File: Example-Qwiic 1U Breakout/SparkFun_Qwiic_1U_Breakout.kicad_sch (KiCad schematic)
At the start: 37 parts, among them J1 Qwiic_RA, J2 Qwiic_RA, J3 Conn_01x06, Q1 BSS138, Q2 BSS138, U1 AP3012

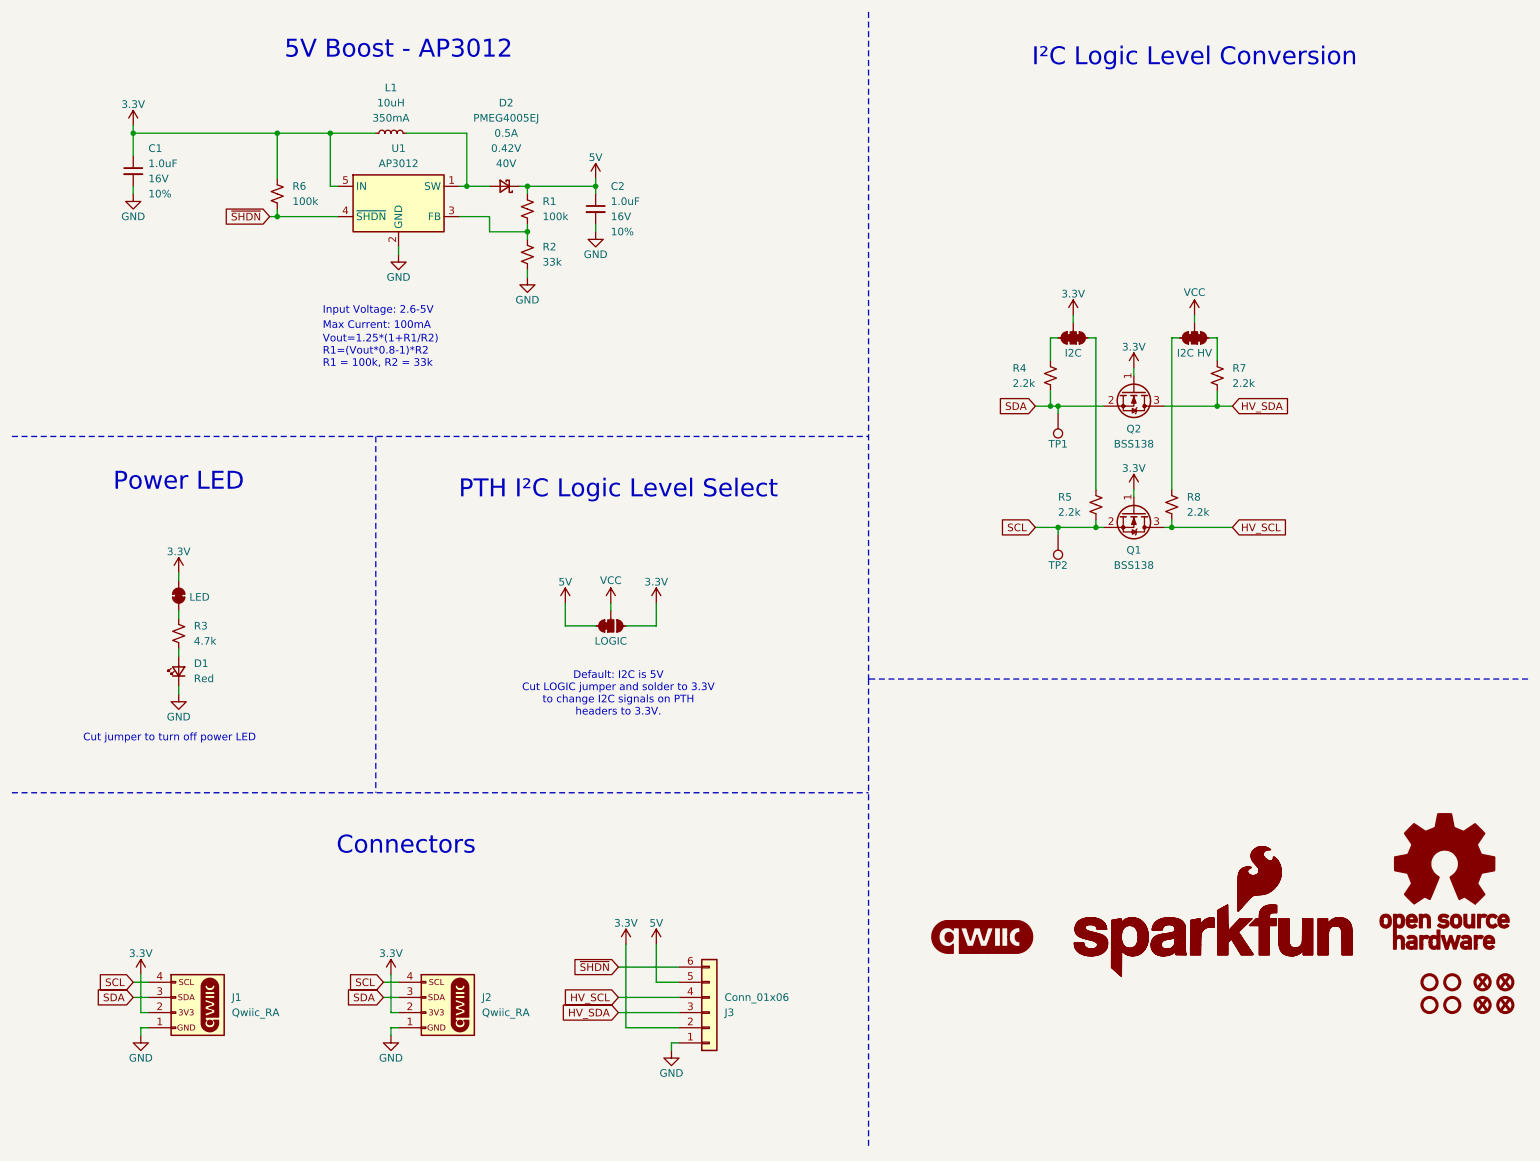
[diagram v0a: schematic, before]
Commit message: Update examples to KiCad v9
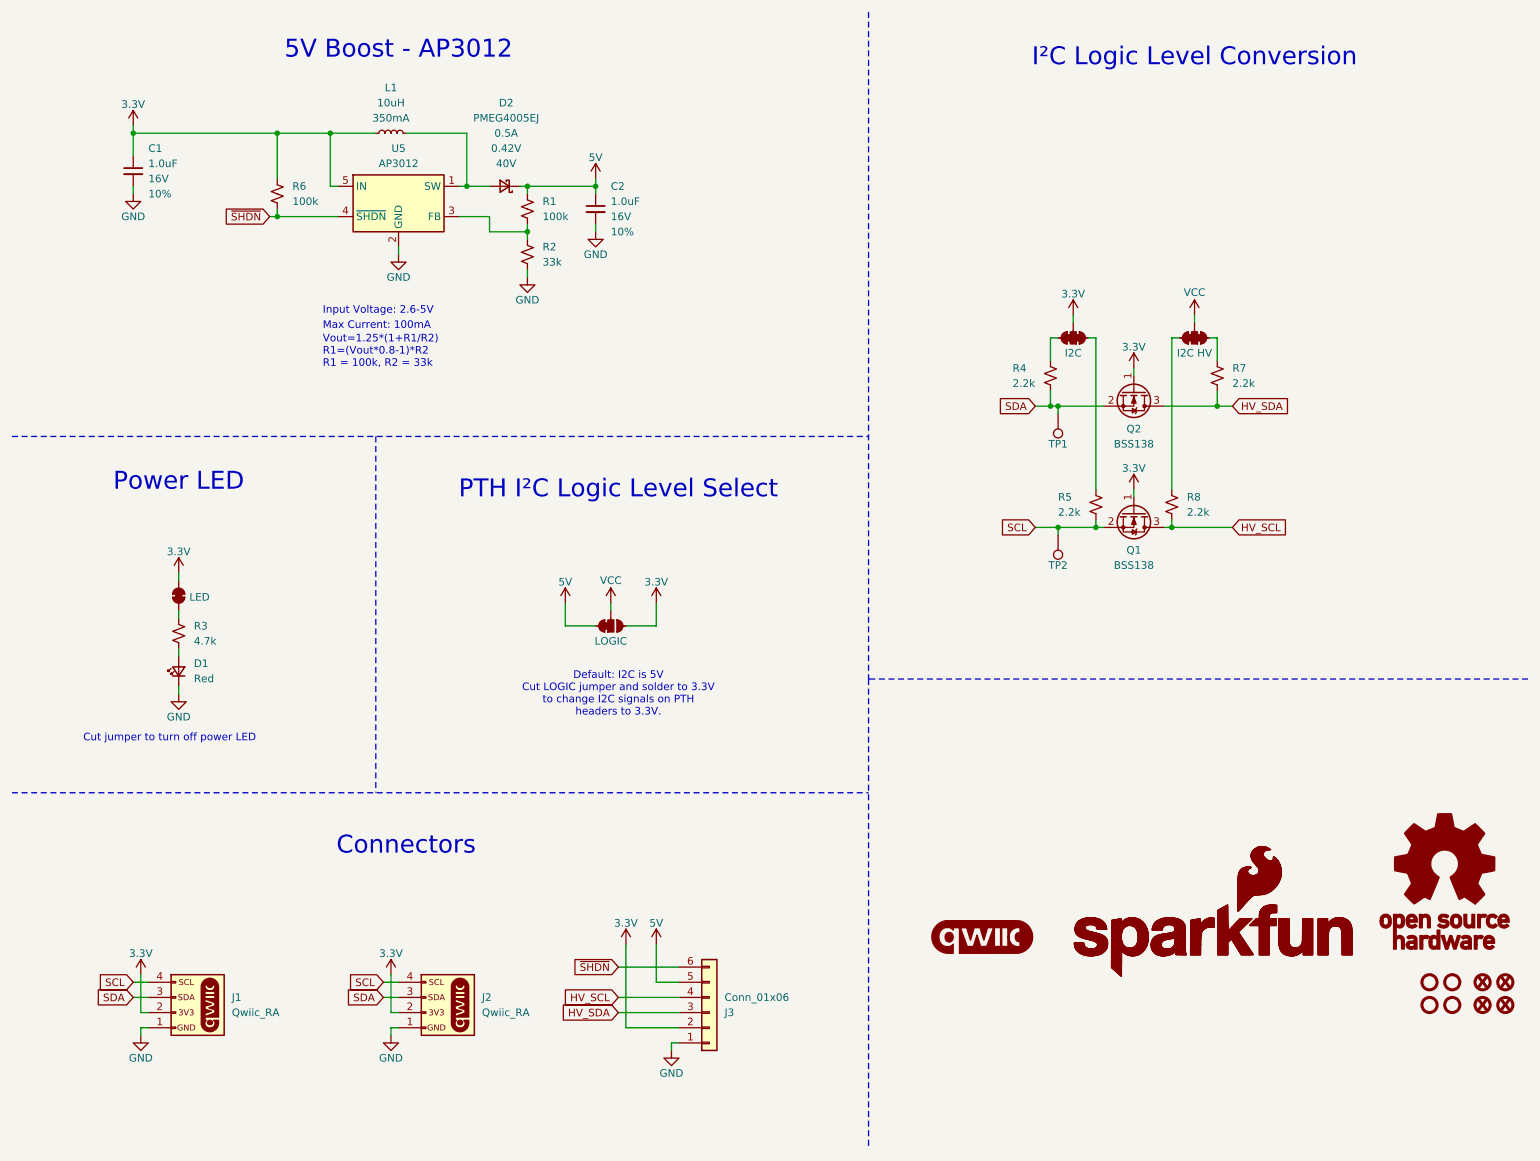
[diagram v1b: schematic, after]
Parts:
- renumbered U1 to U5
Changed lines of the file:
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@@
 (kicad_sch
-	(version 20231120)
+	(version 20250114)
 	(generator "eeschema")
-	(generator_version "8.0")
+	(generator_version "9.0")
 	(paper "USLetter")
 	(title_block
@@
 		(comment 3 "Designed by: P. Lewis")
 	)
+	(text "Input Voltage: 2.6-5V"
+		(exclude_from_sim no)
+		(at 64.77 63.5 0)
+		(effects
+			(font
+				(size 1.27 1.27)
+				(color 132 132 132 1)
+			)
+			(justify left bottom)
+		)
+	)
+	(text "Vout=1.25*(1+R1/R2)\nR1=(Vout*0.8-1)*R2\nR1 = 100k, R2 = 33k"
+		(exclude_from_sim no)
+		(at 64.77 72.39 0)
+		(effects
+			(font
+				(size 1.27 1.27)
+				(color 132 132 132 1)
+			)
+			(justify left bottom)
+		)
+	)
+	(text "Default: I2C is 5V\nCut LOGIC jumper and solder to 3.3V\nto change I2C signals on PTH \nheaders to 3.3V."
+		(exclude_from_sim no)
+		(at 114.3 127 0)
+		(effects
+			(font
+				(size 1.27 1.27)
+				(color 132 132 132 1)
+			)
+		)
+	)
+	(text "I²C Logic Level Conversion"
+		(exclude_from_sim no)
+		(at 210.82 20.32 0)
+		(effects
+			(font
+				(size 3 3)
+			)
+		)
+	)
+	(text "Max Current: 100mA"
+		(exclude_from_sim no)
+		(at 64.77 66.04 0)
+		(effects
+			(font
+				(size 1.27 1.27)
+				(color 132 132 132 1)
+			)
+			(justify left bottom)
+		)
+	)
+	(text "Cut jumper to turn off power LED"
+		(exclude_from_sim no)
+		(at 24.638 135.128 0)
+		(effects
+			(font
+				(size 1.27 1.27)
+				(color 132 132 132 1)
+			)
+			(justify left bottom)
+		)
+	)
+	(text "Power LED"
+		(exclude_from_sim no)
+		(at 40.64 91.44 0)
+		(effects
+			(font
+				(size 3 3)
+			)
+		)
+	)
+	(text "Connectors"
+		(exclude_from_sim no)
+		(at 78.74 152.4 0)
+		(effects
+			(font
+				(size 3 3)
+			)
+		)
+	)
+	(text "PTH I²C Logic Level Select"
+		(exclude_from_sim no)
+		(at 114.3 92.71 0)
+		(effects
+			(font
+				(size 3 3)
+			)
+		)
+	)
+	(text "5V Boost - AP3012"
+		(exclude_from_sim no)
+		(at 77.47 19.05 0)
+		(effects
+			(font
+				(size 3 3)
+			)
+		)
+	)
 	(junction
 		(at 99.06 49.53)
@@
 		)
 	)
-	(text "Input Voltage: 2.6-5V"
-		(exclude_from_sim no)
-		(at 64.77 63.5 0)
-		(effects
-			(font
-				(size 1.27 1.27)
-				(color 132 132 132 1)
-			)
-			(justify left bottom)
-		)
-	)
-	(text "Vout=1.25*(1+R1/R2)\nR1=(Vout*0.8-1)*R2\nR1 = 100k, R2 = 33k"
-		(exclude_from_sim no)
-		(at 64.77 72.39 0)
-		(effects
-			(font
-				(size 1.27 1.27)
-				(color 132 132 132 1)
-			)
-			(justify left bottom)
-		)
-	)
-	(text "Default: I2C is 5V\nCut LOGIC jumper and solder to 3.3V\nto change I2C signals on PTH \nheaders to 3.3V."
-		(exclude_from_sim no)
-		(at 114.3 127 0)
-		(effects
-			(font
-				(size 1.27 1.27)
-				(color 132 132 132 1)
-			)
-		)
-	)
-	(text "I²C Logic Level Conversion"
-		(exclude_from_sim no)
-		(at 210.82 20.32 0)
-		(effects
-			(font
-				(size 3 3)
-			)
-		)
-	)
-	(text "Max Current: 100mA"
-		(exclude_from_sim no)
-		(at 64.77 66.04 0)
-		(effects
-			(font
-				(size 1.27 1.27)
-				(color 132 132 132 1)
-			)
-			(justify left bottom)
-		)
-	)
-	(text "Cut jumper to turn off power LED"
-		(exclude_from_sim no)
-		(at 24.638 135.128 0)
-		(effects
-			(font
-				(size 1.27 1.27)
-				(color 132 132 132 1)
-			)
-			(justify left bottom)
-		)
-	)
-	(text "Power LED"
-		(exclude_from_sim no)
-		(at 40.64 91.44 0)
-		(effects
-			(font
-				(size 3 3)
-			)
-		)
-	)
-	(text "Connectors"
-		(exclude_from_sim no)
-		(at 78.74 152.4 0)
-		(effects
-			(font
-				(size 3 3)
-			)
-		)
-	)
-	(text "PTH I²C Logic Level Select"
-		(exclude_from_sim no)
-		(at 114.3 92.71 0)
-		(effects
-			(font
-				(size 3 3)
-			)
-		)
-	)
-	(text "5V Boost - AP3012"
-		(exclude_from_sim no)
-		(at 77.47 19.05 0)
-		(effects
-			(font
-				(size 3 3)
-			)
-		)
-	)
 	(global_label "HV_SDA"
 		(shape input)
@@
 		(on_board yes)
 		(dnp no)
-		(property "Reference" "#PWR03"
+		(property "Reference" "#PWR0109"
 			(at 77.47 59.69 0)
 			(effects
@@
 		(on_board yes)
 		(dnp no)
-		(property "Reference" "#PWR04"
+		(property "Reference" "#PWR0101"
 			(at 99.06 63.5 0)
 			(effects
@@
 		(on_board yes)
 		(dnp no)
-		(property "Reference" "#PWR0124"
+		(property "Reference" "#PWR0107"
 			(at 123.19 193.04 0)
 			(effects
@@
 		(dnp no)
 		(fields_autoplaced yes)
-		(property "Reference" "U1"
+		(property "Reference" "U5"
 			(at 77.47 35.56 0)
 			(effects
@@
 		(on_board yes)
 		(dnp no)
-		(property "Reference" "#PWR0124"
+		(property "Reference" "#PWR0123"
 			(at 34.29 190.5 0)
 			(effects
@@
 		(on_board yes)
 		(dnp no)
-		(property "Reference" "#PWR0124"
+		(property "Reference" "#PWR0105"
 			(at 76.2 190.5 0)
 			(effects
@@
 		(on_board yes)
 		(dnp no)
-		(property "Reference" "#PWR05"
+		(property "Reference" "#PWR0102"
 			(at 110.49 55.88 0)
 			(effects
@@
 		(on_board yes)
 		(dnp no)
-		(property "Reference" "#PWR02"
+		(property "Reference" "#PWR0110"
 			(at 33.02 49.53 0)
 			(effects
@@
 		)
 	)
+	(embedded_fonts no)
 )

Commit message: Make text gray. Superscript 2s. Add company name.
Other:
- note added: "5V Boost"
- note added: "Default: I²C is 5V Cut LOGIC jumper and solder to 3.3V to change I²C signals on PTH headers to 3.3V."
- note removed: "5V Boost - AP3012"
- note removed: "Default: I2C is 5V Cut LOGIC jumper and solder to 3.3V to change I2C signals on PTH headers to 3.3V."
- note removed: "PTH I²C Logic Level Select"
- company: (none) -> SparkFun Electronics
- moved on the sheet: C1, C2, D1, D2, J1, J2, J3, Q1, Q2, R1, R2, R3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

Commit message: Update examples with latest parts
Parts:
- J1, J2: footprint SparkFun-Connector:JST_SMD_1.0mm-4_Black -> SparkFun-Connector:JST_1x04_P1.0mm_Horizontal_SMD; symbol SparkFun-Connector:Qwiic_Right_Angle -> SparkFun-Connector:Qwiic_Horizontal
- J3: footprint SparkFun-Connector:1x06 -> SparkFun-Connector:1x06_P2.54mm; symbol SparkFun-Connector:Conn_01x06 -> SparkFun-Connector:Conn_01x06_P2.54mm
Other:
- note added: "Voltage Selection"
- moved on the sheet: J1
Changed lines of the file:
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@@
 		(effects
 			(font
-				(size 2.54 2.54)
+				(size 3 3)
 			)
 		)
@@
 		(effects
 			(font
-				(size 2.54 2.54)
+				(size 3 3)
 			)
 		)
@@
 		(effects
 			(font
-				(size 2.54 2.54)
+				(size 3 3)
 			)
 		)
@@
 		(effects
 			(font
-				(size 2.54 2.54)
+				(size 3 3)
+			)
+		)
+	)
+	(text "Voltage Selection"
+		(exclude_from_sim no)
+		(at 113.03 92.71 0)
+		(effects
+			(font
+				(size 3 3)
 			)
 		)
@@
 	(wire
 		(pts
-			(xy 43.18 179.07) (xy 41.91 179.07)
+			(xy 36.83 179.07) (xy 35.56 179.07)
 		)
 		(stroke
@@
 	(wire
 		(pts
-			(xy 40.64 173.99) (xy 43.18 173.99)
+			(xy 34.29 173.99) (xy 36.83 173.99)
 		)
 		(stroke
@@
 	(wire
 		(pts
-			(xy 43.18 176.53) (xy 41.91 176.53)
+			(xy 36.83 176.53) (xy 35.56 176.53)
 		)
 		(stroke
@@
 	(wire
 		(pts
-			(xy 40.64 171.45) (xy 43.18 171.45)
+			(xy 34.29 171.45) (xy 36.83 171.45)
 		)
 		(stroke
@@
 	(wire
 		(pts
-			(xy 41.91 170.18) (xy 41.91 176.53)
+			(xy 35.56 170.18) (xy 35.56 176.53)
 		)
 		(stroke
@@
 	(wire
 		(pts
-			(xy 41.91 179.07) (xy 41.91 180.34)
+			(xy 35.56 179.07) (xy 35.56 180.34)
 		)
 		(stroke
@@
 	(global_label "SCL"
 		(shape input)
-		(at 40.64 171.45 180)
+		(at 34.29 171.45 180)
 		(fields_autoplaced yes)
 		(effects
@@
 		)
 		(property "Intersheetrefs" "${INTERSHEET_REFS}"
-			(at 34.1472 171.45 0)
+			(at 27.7972 171.45 0)
 			(effects
 				(font
@@
 	(global_label "SDA"
 		(shape input)
-		(at 40.64 173.99 180)
+		(at 34.29 173.99 180)
 		(fields_autoplaced yes)
 		(effects
@@
 		)
 		(property "Intersheetrefs" "${INTERSHEET_REFS}"
-			(at 34.0867 173.99 0)
+			(at 27.7367 173.99 0)
 			(effects
 				(font
@@
 	)
 	(symbol
-		(lib_id "SparkFun-Connector:Conn_01x06")
+		(lib_id "SparkFun-Connector:Conn_01x06_P2.54mm")
 		(at 113.03 173.99 0)
 		(mirror x)
@@
 			)
 		)
-		(property "Footprint" "SparkFun-Connector:1x06"
+		(property "Footprint" "SparkFun-Connector:1x06_P2.54mm"
 			(at 113.03 161.29 0)
 			(effects
@@
 			)
 		)
-		(property "Datasheet" "https://docs.broadcom.com/docs/AV02-0551EN"
+		(property "Datasheet" "https://www.kingbrightusa.com/images/catalog/SPEC/APT1608SURCK.pdf"
 			(at 54.61 124.46 0)
 			(effects
@@
 	(symbol
 		(lib_id "SparkFun-PowerSymbol:GND")
-		(at 41.91 180.34 0)
+		(at 35.56 180.34 0)
 		(unit 1)
 		(exclude_from_sim no)
@@
 		(dnp no)
 		(property "Reference" "#PWR0123"
-			(at 41.91 186.69 0)
+			(at 35.56 186.69 0)
 			(effects
 				(font
@@
 		)
 		(property "Value" "GND"
-			(at 41.91 184.15 0)
+			(at 35.56 184.15 0)
 			(effects
 				(font
@@
 		)
 		(property "Footprint" ""
-			(at 41.91 180.34 0)
+			(at 35.56 180.34 0)
 			(effects
 				(font
@@
 		)
 		(property "Datasheet" ""
-			(at 41.91 180.34 0)
+			(at 35.56 180.34 0)
 			(effects
 				(font
@@
 		)
 		(property "Description" "Power symbol creates a global label with name \"GND\" , ground"
-			(at 41.91 180.34 0)
+			(at 35.56 180.34 0)
 			(effects
 				(font
@@
 	)
 	(symbol
-		(lib_id "SparkFun-Connector:Qwiic_Right_Angle")
-		(at 48.26 173.99 0)
+		(lib_id "SparkFun-Connector:Qwiic_Horizontal")
+		(at 41.91 173.99 0)
 		(unit 1)
 		(exclude_from_sim no)
@@
 		(fields_autoplaced yes)
 		(property "Reference" "J1"
-			(at 51.435 165.1 0)
+			(at 50.8 173.9899 0)
 			(effects
 				(font
 					(size 1.27 1.27)
 				)
+				(justify left)
 			)
 		)
 		(property "Value" "Qwiic_RA"
-			(at 51.435 167.64 0)
+			(at 50.8 176.5299 0)
 			(effects
 				(font
 					(size 1.27 1.27)
 				)
+				(justify left)
 			)
 		)
-		(property "Footprint" "SparkFun-Connector:JST_SMD_1.0mm-4_Black"
-			(at 48.26 186.69 0)
+		(property "Footprint" "SparkFun-Connector:JST_1x04_P1.0mm_Horizontal_SMD"
+			(at 41.91 186.69 0)
 			(effects
 				(font
@@
 		)
 		(property "Datasheet" "https://www.jst-mfg.com/product/pdf/eng/eSH.pdf"
-			(at 48.26 189.23 0)
+			(at 41.91 189.23 0)
 			(effects
 				(font
@@
 		)
 		(property "Description" "4 pin JST 1mm polarized connector for I2C"
-			(at 48.26 173.99 0)
+			(at 41.91 191.77 0)
 			(effects
 				(font
@@
 		)
 		(property "PROD_ID" "CONN-13694"
-			(at 48.26 184.15 0)
+			(at 41.91 184.15 0)
 			(effects
 				(font
@@
 	(symbol
 		(lib_id "SparkFun-PowerSymbol:3.3V")
-		(at 41.91 170.18 0)
+		(at 35.56 170.18 0)
 		(unit 1)
 		(exclude_from_sim no)
@@
 		(dnp no)
 		(property "Reference" "#PWR0124"
-			(at 41.91 173.99 0)
+			(at 35.56 173.99 0)
 			(effects
 				(font
@@
 		)
 		(property "Value" "3.3V"
-			(at 41.91 166.624 0)
+			(at 35.56 166.624 0)
 			(effects
 				(font
@@
 		)
 		(property "Footprint" ""
-			(at 41.91 170.18 0)
+			(at 35.56 170.18 0)
 			(effects
 				(font
@@
 		)
 		(property "Datasheet" ""
-			(at 41.91 170.18 0)
+			(at 35.56 170.18 0)
 			(effects
 				(font
@@
 		)
 		(property "Description" "Power symbol creates a global label with name \"3.3V\""
-			(at 41.91 170.18 0)
+			(at 35.56 170.18 0)
 			(effects
 				(font
@@
 	)
 	(symbol
-		(lib_id "SparkFun-Connector:Qwiic_Right_Angle")
+		(lib_id "SparkFun-Connector:Qwiic_Horizontal")
 		(at 73.66 173.99 0)
 		(unit 1)
@@
 		(fields_autoplaced yes)
 		(property "Reference" "J2"
-			(at 76.835 165.1 0)
+			(at 82.55 173.9899 0)
 			(effects
 				(font
 					(size 1.27 1.27)
 				)
+				(justify left)
 			)
 		)
 		(property "Value" "Qwiic_RA"
-			(at 76.835 167.64 0)
+			(at 82.55 176.5299 0)
 			(effects
 				(font
 					(size 1.27 1.27)
 				)
+				(justify left)
 			)
 		)
-		(property "Footprint" "SparkFun-Connector:JST_SMD_1.0mm-4_Black"
+		(property "Footprint" "SparkFun-Connector:JST_1x04_P1.0mm_Horizontal_SMD"
 			(at 73.66 186.69 0)
 			(effects
@@
 		)
 		(property "Description" "4 pin JST 1mm polarized connector for I2C"
-			(at 73.66 173.99 0)
+			(at 73.66 191.77 0)
 			(effects
 				(font
